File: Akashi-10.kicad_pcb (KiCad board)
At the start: 2 copper layers, 66 x 88 mm, 7 parts, among them J1 Conn_02x20_Odd_Even, J2 Conn_02x20_Odd_Even, J3 Conn_02x20_Counter_Clockwise, P1 EL-210-KEY, U1 9-ST-20

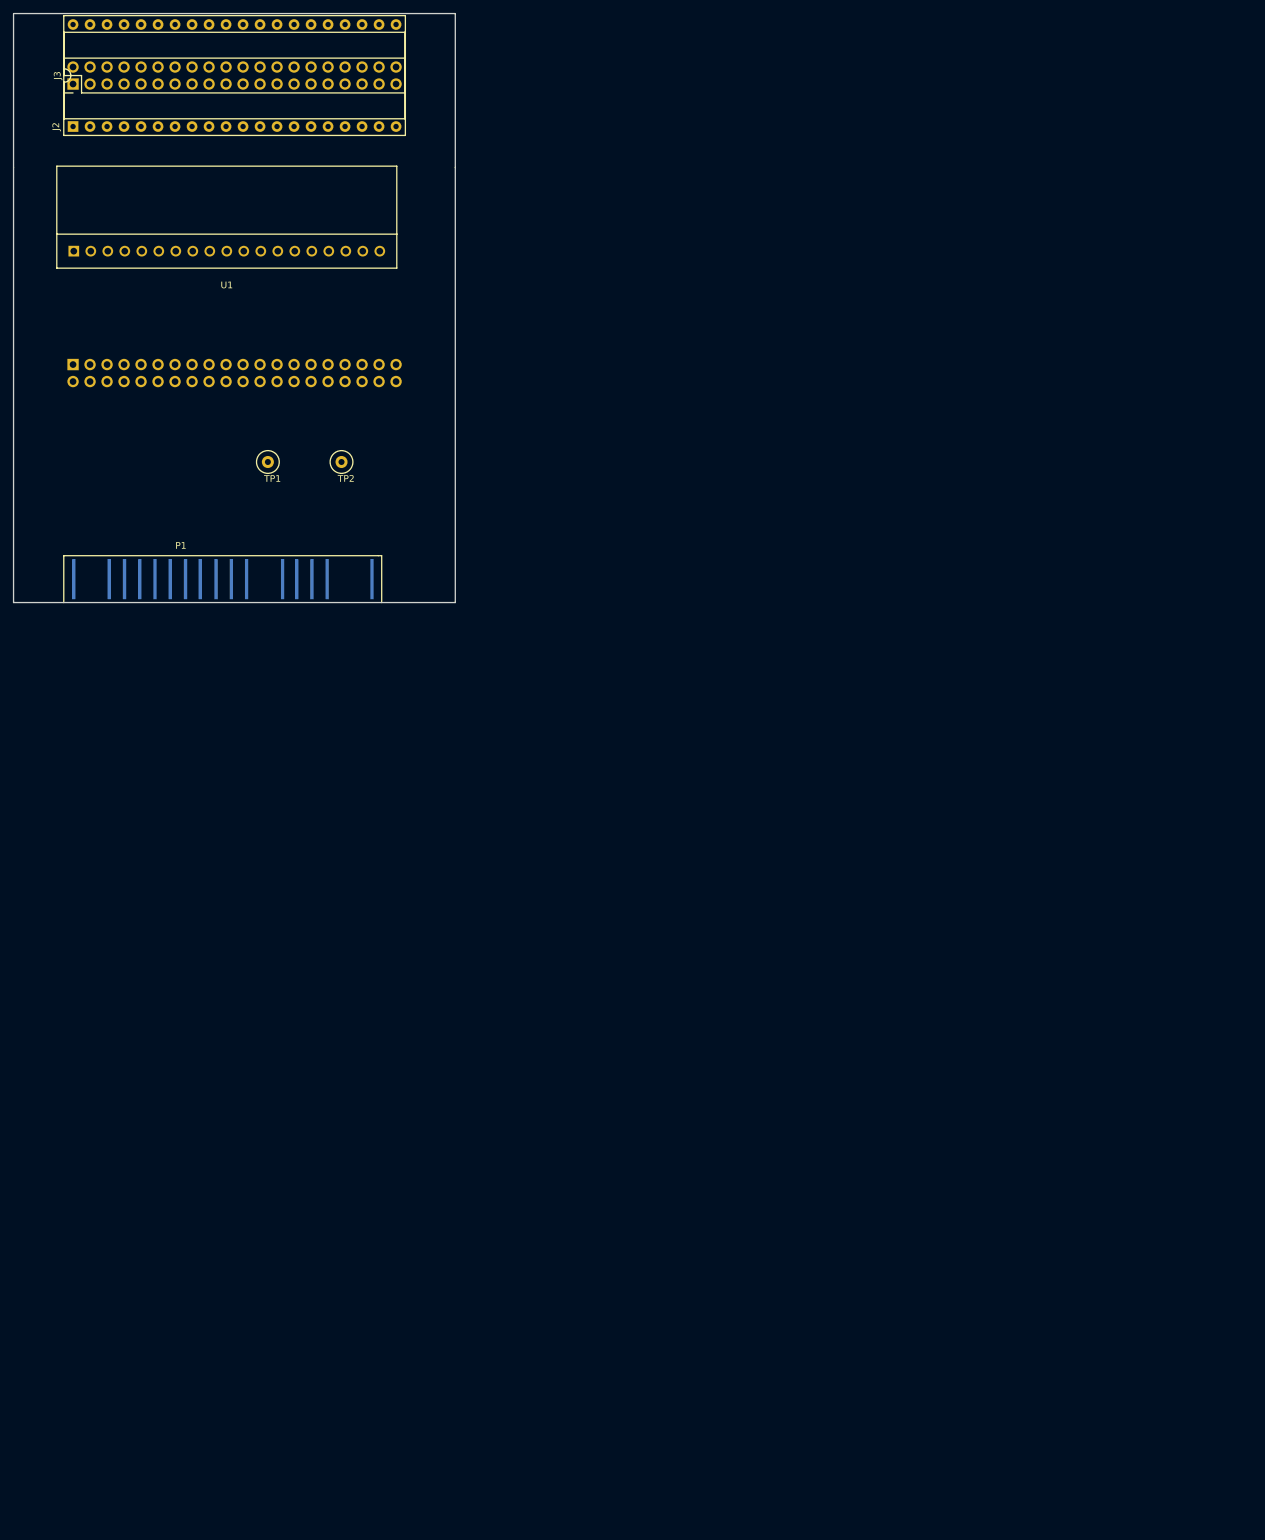
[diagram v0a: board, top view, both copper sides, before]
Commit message: Add holes
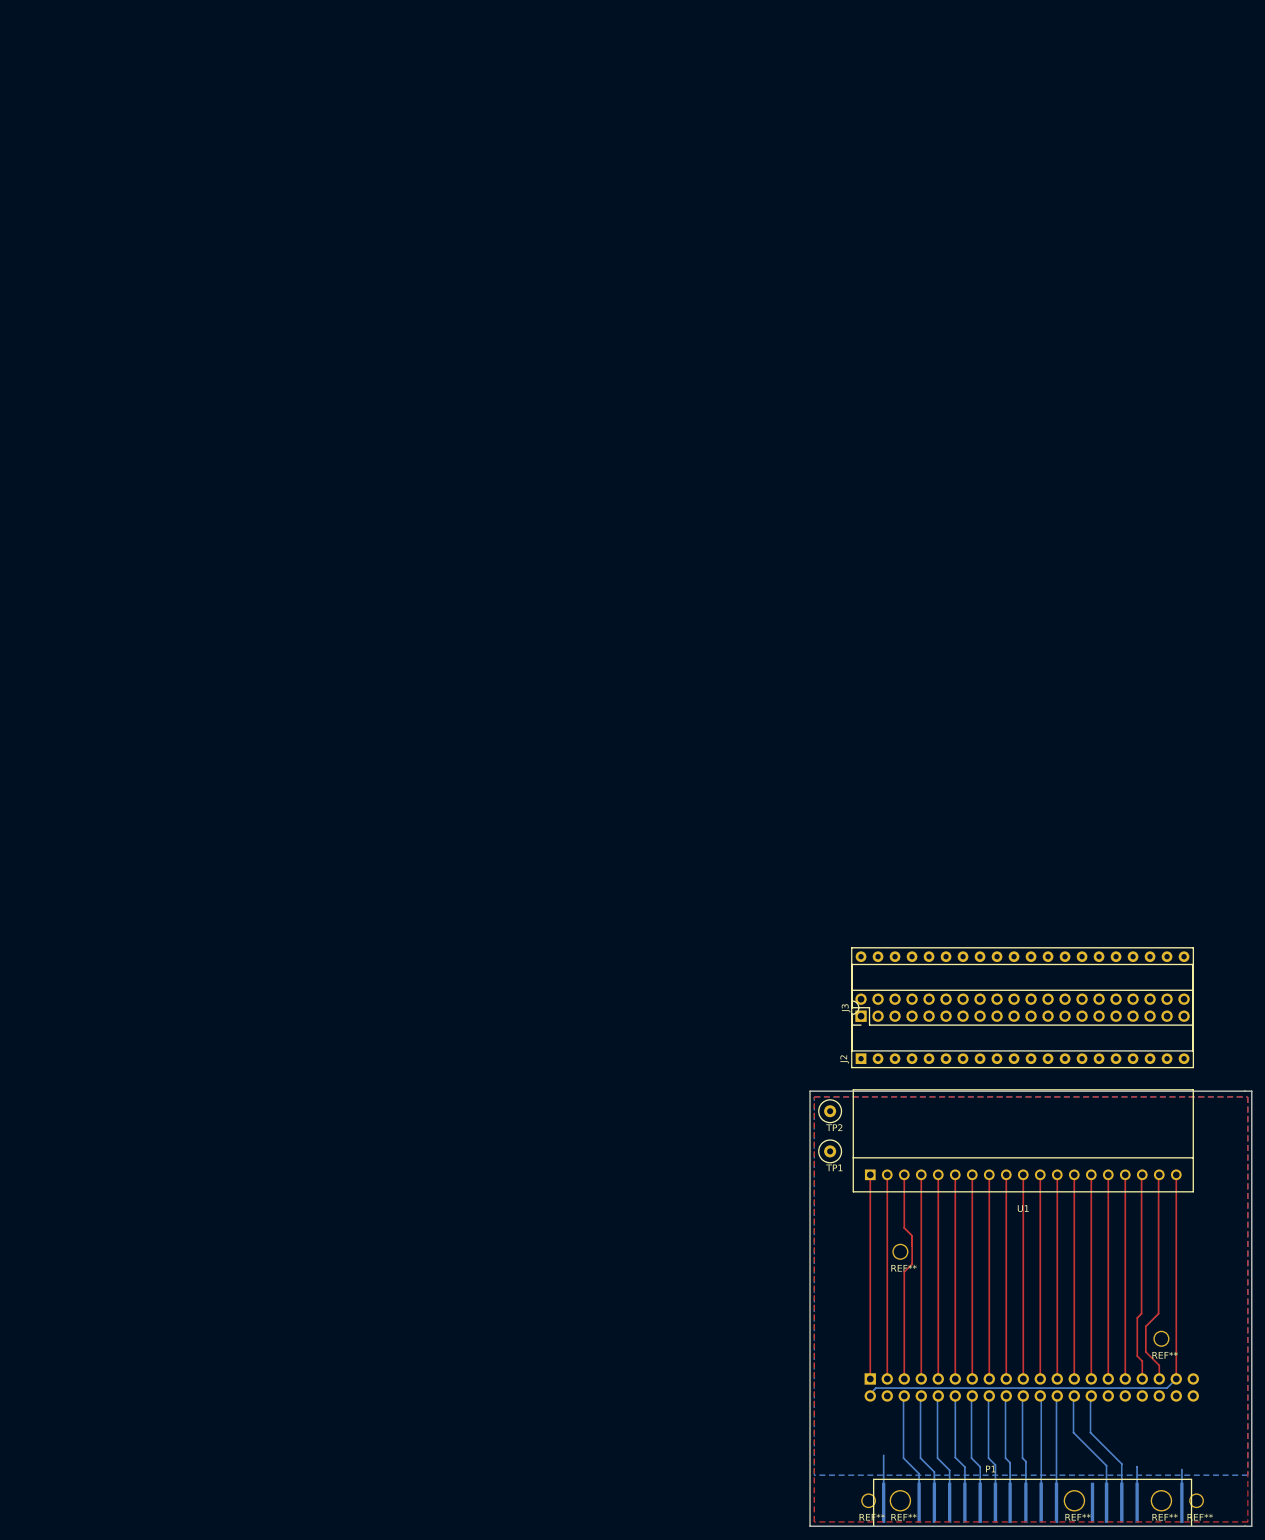
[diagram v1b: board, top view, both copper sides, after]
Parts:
- added REF**: hole_1.8mm, hole:hole_1.8mm, F.Cu at (127.8, 134.2)
- added REF**: hole_1.8mm, hole:hole_1.8mm, F.Cu at (176.8, 134.2)
- added REF**: hole_2.0mm, hole:hole_2.0mm, F.Cu at (132.5, 97.0)
- added REF**: hole_2.0mm, hole:hole_2.0mm, F.Cu at (171.5, 110.0)
- added REF**: hole_2.8mm, hole:hole_2.8mm, F.Cu at (171.5, 134.2)
- added REF**: hole_2.8mm, hole:hole_2.8mm, F.Cu at (158.5, 134.2)
- added REF**: hole_2.8mm, hole:hole_2.8mm, F.Cu at (132.5, 134.2)
- moved J1 192.8 mm to (128.0, 116.0)
- moved P1 183.5 mm to (130.0, 138.0)
- moved J2 182.4 mm to (126.6, 61.8)
- moved J3 182.4 mm to (126.6, 68.2)
- moved U1 182.2 mm to (128.0, 85.5)
- moved TP1 132.9 mm to (122.0, 82.0)
- moved TP2 121.4 mm to (122.0, 76.0)
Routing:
- net Net-(J1-Pad2): track 0.00 -> 77.7 mm
- net Net-(J1-Pad5): track 0.00 -> 32.7 mm
- net Net-(J1-Pad35): track 0.00 -> 31.7 mm
- net Net-(J1-Pad21): track 0.00 -> 31.4 mm
- net Net-(J1-Pad33): track 0.00 -> 31.3 mm
- net Net-(J1-Pad13): track 0.00 -> 31.3 mm
- net Net-(J1-Pad9): track 0.00 -> 31.3 mm
- net Net-(J1-Pad15): track 0.00 -> 31.0 mm
- net Net-(J1-Pad3): track 0.00 -> 31.0 mm
- net Net-(J1-Pad29): track 0.00 -> 30.3 mm
- net Net-(J1-Pad27): track 0.00 -> 30.3 mm
- net Net-(J1-Pad25): track 0.00 -> 30.3 mm
- net Net-(J1-Pad23): track 0.00 -> 30.3 mm
- net Net-(J1-Pad7): track 0.00 -> 30.1 mm
- net Net-(J1-Pad19): track 0.00 -> 30.1 mm
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- added copper zone on F.Cu, net +3V3
- added copper zone on B.Cu, net GND
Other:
- board size 66 x 88 mm -> 66 x 65 mm
- board text added: "3.3v"
- board text added: "GND"

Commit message: All routed
No DRC error
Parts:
- moved J2 6.54 mm to (120.9, 65.0)
- moved J3 6.54 mm to (120.9, 71.3)
- moved TP2 0.91 mm to (122.8, 76.4)
- moved TP1 0.82 mm to (122.8, 82.1)
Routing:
- net Net-(J2-Pad11): track 0.00 -> 7.25 mm
- net Net-(J2-Pad9): track 0.00 -> 6.35 mm
- net Net-(J2-Pad7): track 0.00 -> 6.35 mm
- net Net-(J2-Pad5): track 0.00 -> 6.35 mm
- net Net-(J2-Pad39): track 0.00 -> 6.35 mm
- net Net-(J2-Pad37): track 0.00 -> 6.35 mm
- net Net-(J2-Pad35): track 0.00 -> 6.35 mm
- net Net-(J2-Pad33): track 0.00 -> 6.35 mm
- net Net-(J2-Pad31): track 0.00 -> 6.35 mm
- net Net-(J2-Pad3): track 0.00 -> 6.35 mm
- net Net-(J2-Pad29): track 0.00 -> 6.35 mm
- net Net-(J2-Pad27): track 0.00 -> 6.35 mm
- net Net-(J2-Pad25): track 0.00 -> 6.35 mm
- net Net-(J2-Pad23): track 0.00 -> 6.35 mm
- net Net-(J2-Pad21): track 0.00 -> 6.35 mm
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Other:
- board size 66 x 65 mm -> 66 x 83.5 mm
- board text added: "3.3V"
- board text added: "Akashi-10"
- board text added: "D0"
- board text added: "D1"
- board text added: "D2"
- board text added: "D3"
- board text added: "D4"
- board text added: "D5"
- board text added: "D6"
- board text added: "D7"
- board text added: "D8"
- board text added: "H1"
- board text added: "H2"
- board text added: "K1"
- board text added: "K2"
- board text added: "K3"
- board text added: "VCUT"
- board text added: "a"
- board text added: "b"
- board text added: "c"
- board text added: "d"
- board text added: "dp"
- board text added: "e"
- board text added: "f"
- board text added: "g"
- board text added: "https://github.com/suikan4github/Akashi-10"

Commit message: Add version number to Silk
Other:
- board text added: "Akashi-10 v1.0.0"
- board text removed: "Akashi-10"
